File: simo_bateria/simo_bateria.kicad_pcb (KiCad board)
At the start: 2 copper layers, 24 x 88 mm, 4 parts, among them J1 CONECTOR SALIDA, U2 cargador_bateria, U3 conversor_dc

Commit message: esquemas listos para revisar
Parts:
- added BAT2: bateria, Battery:BatteryHolder_MPD_BH-18650-PC2, F.Cu at (181.0, 45.0)
- U3: moved to F.Cu
- moved U3 20.6 mm to (157.5, 65.5), turned to 0 degrees
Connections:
- BAT1 pad 1: Net-(BAT1-Pad1) -> unconnected-(BAT1-Pad1)
- BAT1 pad 2: Net-(BAT1-Pad2) -> unconnected-(BAT1-Pad2)
- J1 pad 3: Net-(BAT1-Pad1) -> unconnected-(J1-Pad3)
- U2 pad 2: Net-(BAT1-Pad2) -> unconnected-(U2-Pad2)
- U2 pad 6: Net-(BAT1-Pad1) -> unconnected-(U2-Pad6)
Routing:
- net unconnected-(BAT1-Pad1): track 0.00 -> 99.2 mm
- net Net-(BAT1-Pad1): track 99.2 -> 0.00 mm
- net unconnected-(BAT1-Pad2): track 0.00 -> 47.5 mm
- net Net-(BAT1-Pad2): track 47.5 -> 0.00 mm
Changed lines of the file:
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@@
   (net 3 "unconnected-(U2-Pad4)")
   (net 4 "Net-(U2-Pad5)")
-  (net 5 "Net-(BAT1-Pad1)")
-  (net 6 "Net-(BAT1-Pad2)")
+  (net 5 "unconnected-(BAT1-Pad1)")
+  (net 6 "unconnected-(BAT1-Pad2)")
   (net 7 "+BATT")
   (net 8 "GND")
+  (net 9 "unconnected-(BAT2-Pad1)")
+  (net 10 "unconnected-(BAT2-Pad2)")
+  (net 11 "unconnected-(J1-Pad3)")
+  (net 12 "unconnected-(U2-Pad2)")
+  (net 13 "unconnected-(U2-Pad6)")
   (footprint "Battery:BatteryHolder_MPD_BH-18650-PC2" (layer "F.Cu")
     (at 130 31 -90)
@@
     (pad "" np_thru_hole circle (at 8.645 0 270) (size 3.2 3.2) (drill 3.2) (layers *.Cu *.Mask))
     (pad "1" thru_hole rect (at 0 0 270) (size 3.5 3.5) (drill 2) (layers *.Cu *.Mask)
-      (net 5 "Net-(BAT1-Pad1)") (pinfunction "VBAT+") (pintype "power_in"))
+      (net 5 "unconnected-(BAT1-Pad1)") (pinfunction "VBAT+") (pintype "power_in"))
     (pad "2" thru_hole circle (at 72 0 270) (size 3.5 3.5) (drill 2) (layers *.Cu *.Mask)
-      (net 6 "Net-(BAT1-Pad2)") (pinfunction "VBAT-") (pintype "power_in"))
+      (net 6 "unconnected-(BAT1-Pad2)") (pinfunction "VBAT-") (pintype "power_in"))
     (model "${KIPRJMOD}/Battery.3dshapes/BatteryHolder_MPD_BH-18650-PC2.step"
       (offset (xyz 0 0 0))
@@
       (net 8 "GND") (pinfunction "Pin_2") (pintype "passive"))
     (pad "3" thru_hole oval (at 5 0) (size 1.7 1.95) (drill 0.95) (layers *.Cu *.Mask)
-      (net 5 "Net-(BAT1-Pad1)") (pinfunction "Pin_3") (pintype "passive"))
+      (net 11 "unconnected-(J1-Pad3)") (pinfunction "Pin_3") (pintype "passive"))
     (model "${KICAD6_3DMODEL_DIR}/Connector_JST.3dshapes/JST_EH_B3B-EH-A_1x03_P2.50mm_Vertical.wrl"
       (offset (xyz 0 0 0))
@@
     )
   )
-  (footprint "simo_bateria:conversor_dc_dc" (layer "B.Cu")
-    (at 137 67 180)
-    (property "Sheetfile" "simo_bateria.kicad_sch")
-    (property "Sheetname" "")
-    (attr through_hole)
-    (fp_text reference "U3" (at 7.3 -13.1) (layer "B.SilkS")
-      (effects (font (size 1 1) (thickness 0.15)) (justify mirror))
-    )
-    (fp_text value "conversor_dc" (at 7.4 -8.8) (layer "B.Fab")
-      (effects (font (size 1 1) (thickness 0.15)) (justify mirror))
-    )
-    (fp_text user "IN-" (at 0.4 -3.1) (layer "B.SilkS")
-      (effects (font (size 1 1) (thickness 0.15)) (justify mirror))
-    )
-    (fp_text user "OUT+" (at 14 -22.5 90) (layer "B.SilkS")
-      (effects (font (size 1 1) (thickness 0.15)) (justify mirror))
-    )
-    (fp_text user "OUT-" (at 0 -22.4 90) (layer "B.SilkS")
-      (effects (font (size 1 1) (thickness 0.15)) (justify mirror))
-    )
-    (fp_text user "IN+" (at 13.5 -2.7) (layer "B.SilkS")
-      (effects (font (size 1 1) (thickness 0.15)) (justify mirror))
-    )
-    (fp_text user "POT" (at 10 -18 unlocked) (layer "B.SilkS")
-      (effects (font (size 1 1) (thickness 0.15)) (justify mirror))
-    )
-    (fp_line (start 15.3 1.7) (end 15.3 -28.1) (layer "B.SilkS") (width 0.12))
-    (fp_line (start -1.3 -28.1) (end 15.3 -28.1) (layer "B.SilkS") (width 0.12))
-    (fp_line (start -1.3 1.7) (end 15.3 1.7) (layer "B.SilkS") (width 0.12))
-    (fp_line (start -1.3 1.7) (end -1.3 -28.1) (layer "B.SilkS") (width 0.12))
-    (fp_rect (start 15.3 -11) (end 5 -25) (layer "B.SilkS") (width 0.12) (fill none))
-    (pad "1" thru_hole rect (at 0 0 180) (size 2 2) (drill 1.5) (layers *.Cu *.Mask)
+  (footprint "Battery:BatteryHolder_MPD_BH-18650-PC2" (layer "F.Cu")
+    (at 181 45)
+    (descr "18650 Battery Holder (http://www.memoryprotectiondevices.com/datasheets/BK-18650-PC2-datasheet.pdf)")
+    (tags "18650 Battery Holder")
+    (property "Sheetfile" "simo_bateria.kicad_sch")
+    (property "Sheetname" "")
+    (attr through_hole)
+    (fp_text reference "BAT2" (at 36 1) (layer "F.SilkS")
+      (effects (font (size 1 1) (thickness 0.15)))
+    )
+    (fp_text value "bateria" (at 36 -0.8) (layer "F.Fab")
+      (effects (font (size 1 1) (thickness 0.15)))
+    )
+    (fp_text user "${REFERENCE}" (at 36 -2.4) (layer "F.Fab")
+      (effects (font (size 1 1) (thickness 0.15)))
+    )
+    (fp_line (start 75 -10.05) (end 75 10.05) (layer "F.SilkS") (width 0.12))
+    (fp_line (start -3 -10.05) (end 75 -10.05) (layer "F.SilkS") (width 0.12))
+    (fp_line (start 75 10.05) (end -3 10.05) (layer "F.SilkS") (width 0.12))
+    (fp_line (start -3 10.05) (end -3 -10.05) (layer "F.SilkS") (width 0.12))
+    (fp_line (start 75.2 -10.25) (end 75.2 10.25) (layer "F.CrtYd") (width 0.05))
+    (fp_line (start 75.2 10.25) (end -3.2 10.25) (layer "F.CrtYd") (width 0.05))
+    (fp_line (start -3.2 -10.25) (end 75.2 -10.25) (layer "F.CrtYd") (width 0.05))
+    (fp_line (start -3.2 10.25) (end -3.2 -10.25) (layer "F.CrtYd") (width 0.05))
+    (fp_line (start -2.8 9.85) (end -2.8 -9.85) (layer "F.Fab") (width 0.1))
+    (fp_line (start -2.8 -9.85) (end 74.8 -9.85) (layer "F.Fab") (width 0.1))
+    (fp_line (start 74.8 9.85) (end -2.8 9.85) (layer "F.Fab") (width 0.1))
+    (fp_line (start 74.8 -9.85) (end 74.8 9.85) (layer "F.Fab") (width 0.1))
+    (pad "" np_thru_hole circle (at 64.255 0) (size 3.2 3.2) (drill 3.2) (layers *.Cu *.Mask))
+    (pad "" np_thru_hole circle (at 8.645 0) (size 3.2 3.2) (drill 3.2) (layers *.Cu *.Mask))
+    (pad "1" thru_hole rect (at 0 0) (size 3.5 3.5) (drill 2) (layers *.Cu *.Mask)
+      (net 9 "unconnected-(BAT2-Pad1)") (pinfunction "VBAT+") (pintype "power_in"))
+    (pad "2" thru_hole circle (at 72 0) (size 3.5 3.5) (drill 2) (layers *.Cu *.Mask)
+      (net 10 "unconnected-(BAT2-Pad2)") (pinfunction "VBAT-") (pintype "power_in"))
+    (model "${KICAD6_3DMODEL_DIR}/Battery.3dshapes/BatteryHolder_MPD_BH-18650-PC2.wrl"
+      (offset (xyz 0 0 0))
+      (scale (xyz 1 1 1))
+      (rotate (xyz 0 0 0))
+    )
+  )
+  (footprint "simo_bateria:conversor_dc_dc" (layer "F.Cu")
+    (at 157.5 65.5)
+    (property "Sheetfile" "simo_bateria.kicad_sch")
+    (property "Sheetname" "")
+    (attr through_hole)
+    (fp_text reference "U3" (at 14.4 13.1) (layer "F.SilkS")
+      (effects (font (size 1 1) (thickness 0.15)))
+    )
+    (fp_text value "conversor_dc" (at 7.4 8.8) (layer "F.Fab")
+      (effects (font (size 1 1) (thickness 0.15)))
+    )
+    (fp_text user "POT" (at 17.1 18 unlocked) (layer "F.SilkS")
+      (effects (font (size 1 1) (thickness 0.15)))
+    )
+    (fp_text user "OUT-" (at 0.9 36.3 180) (layer "F.SilkS")
+      (effects (font (size 1 1) (thickness 0.15)))
+    )
+    (fp_text user "IN+" (at 17.5 2.7) (layer "F.SilkS")
+      (effects (font (size 1 1) (thickness 0.15)))
+    )
+    (fp_text user "OUT+" (at 16.7 36.4 180) (layer "F.SilkS")
+      (effects (font (size 1 1) (thickness 0.15)))
+    )
+    (fp_text user "IN-" (at 0.4 3.1) (layer "F.SilkS")
+      (effects (font (size 1 1) (thickness 0.15)))
+    )
+    (fp_line (start -1.3 -1.7) (end -1.3 28.1) (layer "F.SilkS") (width 0.12))
+    (fp_line (start -1.3 39.8) (end -1.3 40.8) (layer "F.SilkS") (width 0.12))
+    (fp_line (start 18.7 28.1) (end 18.7 38.6) (layer "F.SilkS") (width 0.12))
+    (fp_line (start -1.3 38.6) (end -1.3 39.8) (layer "F.SilkS") (width 0.12))
+    (fp_line (start 18.7 -1.7) (end 18.7 28.1) (layer "F.SilkS") (width 0.12))
+    (fp_line (start -1.3 -1.7) (end -1.3 38.6) (layer "F.SilkS") (width 0.12))
+    (fp_line (start 18.7 -1.7) (end -1.3 -1.7) (layer "F.SilkS") (width 0.12))
+    (fp_line (start 18.7 38.6) (end 18.7 39.8) (layer "F.SilkS") (width 0.12))
+    (fp_line (start -1.3 40.8) (end 18.7 40.8) (layer "F.SilkS") (width 0.12))
+    (fp_line (start 18.7 40.8) (end 18.7 39.8) (layer "F.SilkS") (width 0.12))
+    (fp_rect (start 18.55 10.8) (end 8.25 24.8) (layer "F.SilkS") (width 0.12) (fill none))
+    (pad "1" thru_hole rect (at 0 0) (size 2.5 3.25) (drill 1.5) (layers *.Cu *.Mask)
       (net 4 "Net-(U2-Pad5)") (pinfunction "VIN-") (pintype "power_in"))
-    (pad "2" thru_hole rect (at 0 -26.4 180) (size 2 2) (drill 1.5) (layers *.Cu *.Mask)
+    (pad "2" thru_hole rect (at 0 39.1) (size 2.5 3.25) (drill 1.5) (layers *.Cu *.Mask)
       (net 8 "GND") (pinfunction "VOUT-") (pintype "power_out"))
-    (pad "3" thru_hole rect (at 14 0 180) (size 2 2) (drill 1.5) (layers *.Cu *.Mask)
+    (pad "3" thru_hole rect (at 17.5 0) (size 2.5 3.25) (drill 1.5) (layers *.Cu *.Mask)
       (net 2 "Net-(U2-Pad3)") (pinfunction "VIN+") (pintype "power_in"))
-    (pad "4" thru_hole rect (at 14.1 -26.4 180) (size 2 2) (drill 1.5) (layers *.Cu *.Mask)
+    (pad "4" thru_hole rect (at 17.4 39.1) (size 2.5 3.25) (drill 1.5) (layers *.Cu *.Mask)
       (net 7 "+BATT") (pinfunction "VOUT+") (pintype "power_out"))
+    (model "/home/gvelardez/simo_pcb/YAAJ_DCDC_StepDown_LM2596_cp.step"
+      (offset (xyz 17 1.5 0))
+      (scale (xyz 1 1 1))
+      (rotate (xyz 0 0 90))
+    )
   )
   (footprint "simo_bateria:cargador_bat" (layer "B.Cu")
@@
       (net 1 "unconnected-(U2-Pad1)") (pinfunction "IN-") (pintype "power_in+no_connect"))
     (pad "2" thru_hole rect (at 0 -23.6 180) (size 2 2) (drill 1.5) (layers *.Cu *.Mask)
-      (net 6 "Net-(BAT1-Pad2)") (pinfunction "OUT-") (pintype "power_out"))
+      (net 12 "unconnected-(U2-Pad2)") (pinfunction "OUT-") (pintype "power_out"))
     (pad "3" thru_hole rect (at 3 -23.6 180) (size 2 2) (drill 1.5) (layers *.Cu *.Mask)
       (net 2 "Net-(U2-Pad3)") (pinfunction "LOAD-") (pintype "power_out"))
@@
       (net 4 "Net-(U2-Pad5)") (pinfunction "LOAD+") (pintype "power_out"))
     (pad "6" thru_hole rect (at 14.8 -23.6 180) (size 2 2) (drill 1.5) (layers *.Cu *.Mask)
-      (net 5 "Net-(BAT1-Pad1)") (pinfunction "OUT+") (pintype "power_out"))
+      (net 13 "unconnected-(U2-Pad6)") (pinfunction "OUT+") (pintype "power_out"))
   )
   (gr_rect (start 118 26) (end 142 114) (layer "Edge.Cuts") (width 0.1) (fill none))

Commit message: update simo_bateria
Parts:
- removed BAT1, BAT2: bateria, Battery:BatteryHolder_MPD_BH-18650-PC2
- removed U2: cargador_bateria, simo_bateria:cargador_bat
- removed U3: conversor_dc, simo_bateria:conversor_dc_dc
- added 11: conversor_dc_1_1, simo_bateria:conversor_dc_dc, F.Cu at (231.0, 49.5)
- added BT1: Battery_Cell, simo_bateria:BatteryHolder_MPD_BH-18650-PC2, F.Cu at (153.4, 58.0)
- added BT2: Battery_Cell, simo_bateria:BatteryHolder_MPD_BH-18650-PC2, F.Cu at (153.4, 79.6)
- added J2: CONECTOR PLUG IN (5V), Connector_JST:JST_EH_B2B-EH-A_1x02_P2.50mm_Vertical, F.Cu at (153.2, 93.0)
- J1: value CONECTOR SALIDA -> CONECTOR BATERIA( 8V); footprint Connector_JST:JST_EH_B3B-EH-A_1x03_P2.50mm_Vertical -> Connector_JST:JST_EH_B2B-EH-A_1x02_P2.50mm_Vertical
- moved J1 38.2 mm to (162.8, 93.0)
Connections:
- J1 pad 1: +BATT -> Net-(11-Pad3)
- J1 pad 2: GND -> Net-(11-Pad1)
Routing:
- net unconnected-(BAT1-Pad1): track 99.2 -> 0.00 mm
- net unconnected-(BAT1-Pad2): track 47.5 -> 0.00 mm
- net Net-(U2-Pad5): track 27.6 -> 0.00 mm
- net GND: track 18.0 -> 0.00 mm
- net +BATT: track 17.4 -> 0.00 mm
- net Net-(U2-Pad3): track 15.5 -> 0.00 mm
- added copper zone on B.Cu, net (none)
- removed copper zone on B.Cu, net GND

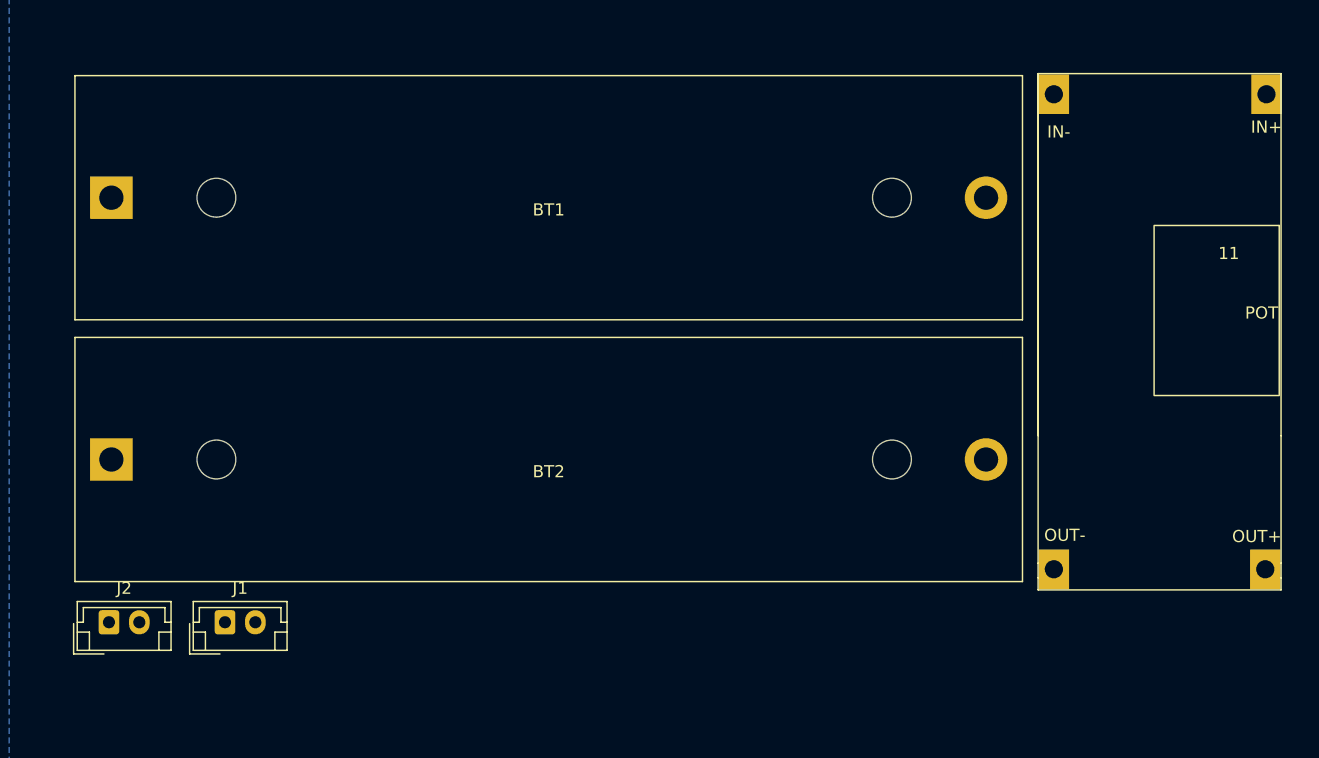
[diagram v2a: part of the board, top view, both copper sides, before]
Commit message: update en ambas placas. Cambio de formato de carpetas. Footprint asignado pero modelos 3d aun no.
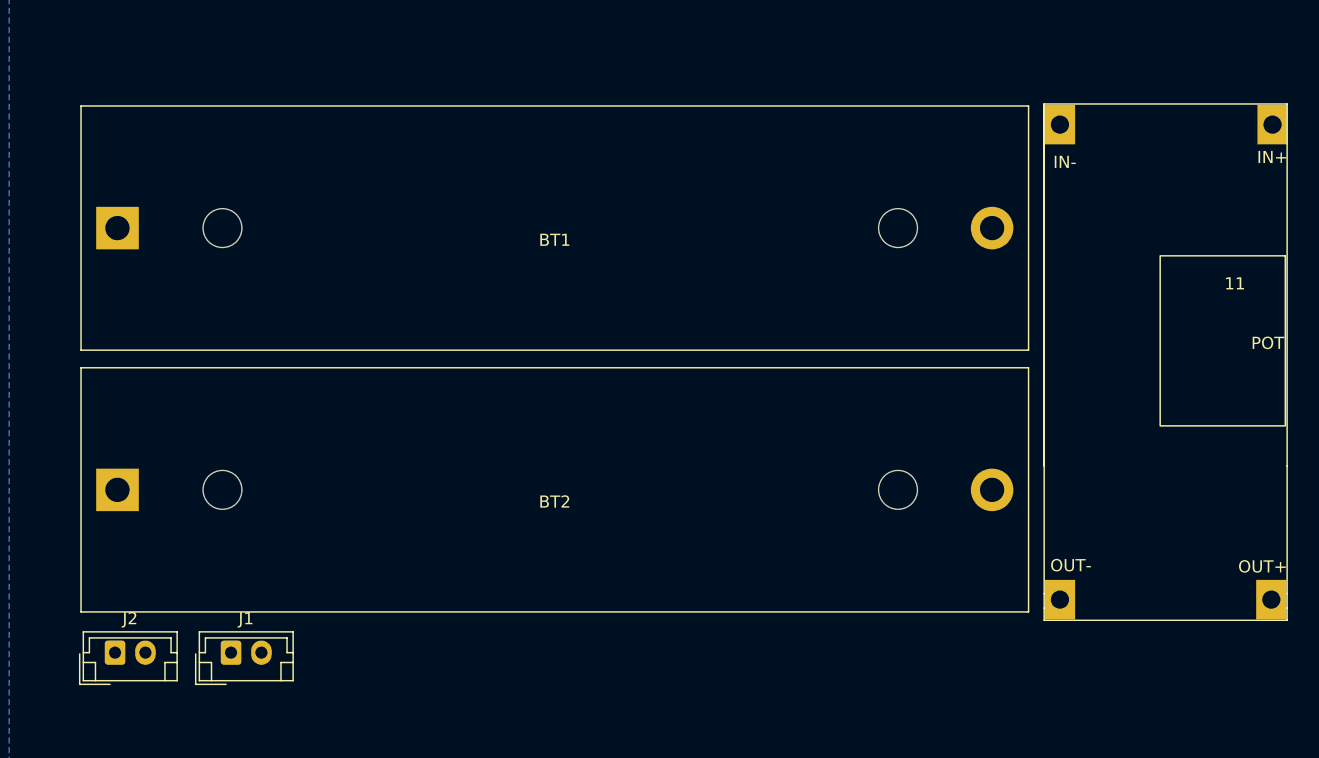
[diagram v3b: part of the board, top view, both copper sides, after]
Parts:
- moved 11 2.55 mm to (231.5, 52.0)
- moved BT1 2.55 mm to (153.9, 60.5)
- moved BT2 2.55 mm to (153.9, 82.1)
- moved J1 2.55 mm to (163.3, 95.5)
- moved J2 2.55 mm to (153.7, 95.5)

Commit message: update en ambas placas, revision 02
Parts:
- removed 11: conversor_dc_1_1, simo_bateria:conversor_dc_dc
- added J1: conector_bateria, simo_bateria:JST_EH_B2B-EH-A_1x02_P2.50mm_Vertical, F.Cu at (255.5, 36.0)
- added J2: conector_bateria, simo_bateria:JST_EH_B2B-EH-A_1x02_P2.50mm_Vertical, F.Cu at (245.9, 36.0)
- added R1: 355k, Resistor_SMD:R_0805_2012Metric_Pad1.20x1.40mm_HandSolder, F.Cu at (184.5, 96.0)
- added R2: 155k, Resistor_SMD:R_0805_2012Metric_Pad1.20x1.40mm_HandSolder, F.Cu at (179.8, 96.0)
- added U1: conversor_dc_1_1, simo_bateria:conversor_dc_dc, F.Cu at (234.0, 51.0)
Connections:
- BT2 pad 2: Net-(11-Pad1) -> Net-(BT2-Pad2)
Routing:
- removed copper zone on B.Cu, net (none)

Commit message: update 2. Listo para revision 2
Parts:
- removed the J1 at (163.3, 95.5)
- removed the J2 at (153.7, 95.5)
- R1, R2, U1: moved to B.Cu
- moved J2 152.3 mm to (115.5, 114.6)
- moved J1 145.8 mm to (132.6, 114.3)
- moved U1 99.9 mm to (134.1, 53.9), turned to 180 degrees
- moved R1 81.6 mm to (122.0, 43.5), turned to -90 degrees
- moved R2 72.7 mm to (129.5, 43.5), turned to 90 degrees
- moved BT1 62.6 mm to (113.8, 108.5), turned to 90 degrees
- moved BT2 32.3 mm to (135.4, 108.5), turned to 90 degrees
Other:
- board size 24 x 88 mm -> 40.5 x 90 mm

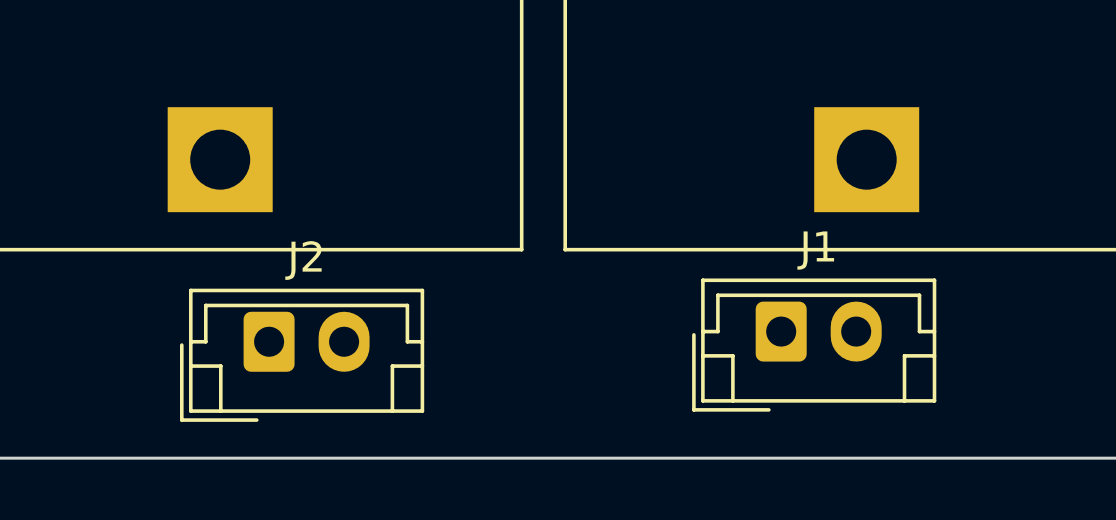
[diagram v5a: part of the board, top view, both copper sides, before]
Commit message: Placa simo bateria: Se modificaron conectores custom en esquema
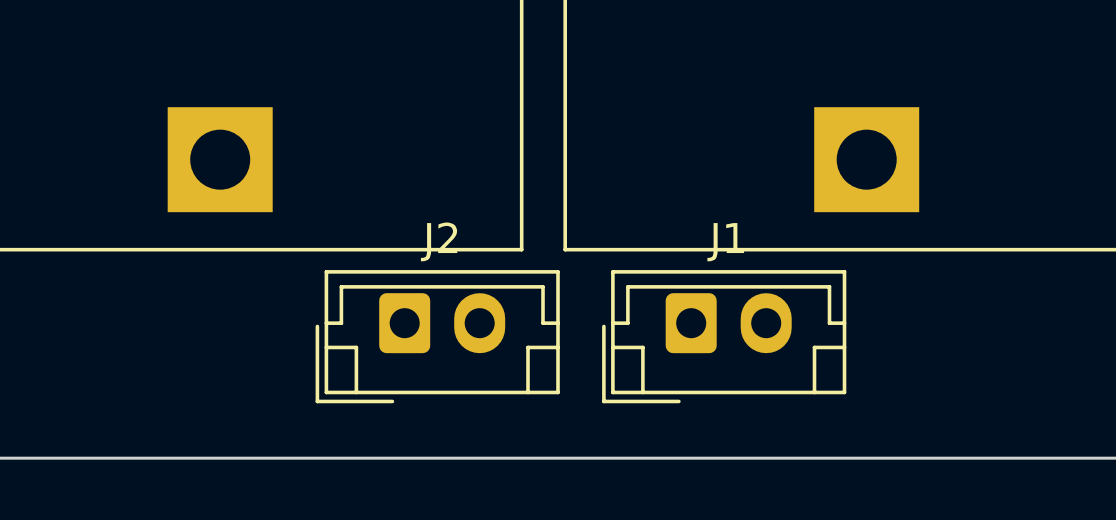
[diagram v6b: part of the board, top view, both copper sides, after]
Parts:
- J1, J2: value conector_bateria -> Conn_01x02_Male
- R1, R2: footprint Resistor_SMD:R_0805_2012Metric_Pad1.20x1.40mm_HandSolder -> simo_bateria:R_0805_2012Metric_Pad1.20x1.40mm_HandSolder
- moved J2 4.56 mm to (120.0, 114.0)
- moved J1 3.01 mm to (129.6, 114.0)
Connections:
- BT1 pad 1: Net-(11-Pad3) -> Net-(BT1-Pad1)
- J1 pad 1: Net-(BT1-Pad1) -> Net-(BT2-Pad2)
- J1 pad 2: Net-(BT2-Pad2) -> Net-(R1-Pad2)
- J2 pad 1: Net-(J2-Pad1) -> Net-(U1-Pad2)
- J2 pad 2: Net-(J2-Pad2) -> Net-(U1-Pad4)
- U1 pad 2: Net-(J2-Pad2) -> Net-(U1-Pad2)
- U1 pad 4: Net-(J2-Pad1) -> Net-(U1-Pad4)
